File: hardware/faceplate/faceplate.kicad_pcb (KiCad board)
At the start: 2 copper layers, 9.8 x 128.5 mm, 10 parts

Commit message: New faceplate
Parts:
- removed REF** (x8): PJ398_faceplate_hole, ModularMountingKit:PJ398_faceplate_hole
- removed REF** (x2): EuroRack_MountingHole, ModularMountingKit:EuroRack_MountingHole
- added H1: Jack 1, ModularMountingHoles:6mm_Jack, F.Cu at (54.9, 66.5)
- added H10: MountingHole, ModularMountingHoles:Eurorack_mounting_hole, F.Cu at (54.0, 175.5)
- added H2: Jack 2, ModularMountingHoles:6mm_Jack, F.Cu at (54.9, 80.4)
- added H3: Jack 3, ModularMountingHoles:6mm_Jack, F.Cu at (54.9, 94.2)
- added H4: Jack 4, ModularMountingHoles:6mm_Jack, F.Cu at (54.9, 108.0)
- added H5: Jack 5, ModularMountingHoles:6mm_Jack, F.Cu at (54.9, 121.8)
- added H6: Jack 6, ModularMountingHoles:6mm_Jack, F.Cu at (54.9, 135.7)
- added H7: Jack 7, ModularMountingHoles:6mm_Jack, F.Cu at (54.9, 149.5)
- added H8: Jack 8, ModularMountingHoles:6mm_Jack, F.Cu at (54.9, 163.3)
- added H9: MountingHole, ModularMountingHoles:Eurorack_mounting_hole, F.Cu at (54.0, 53.0)

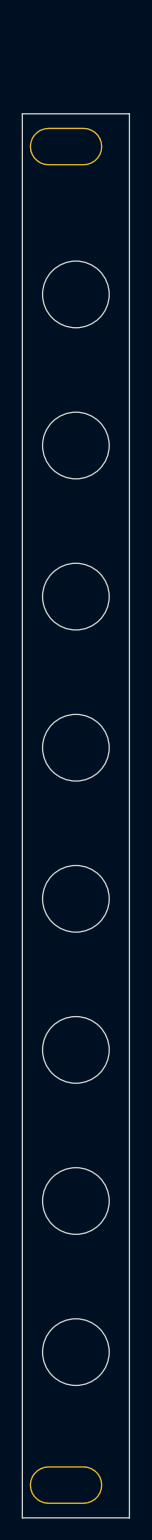
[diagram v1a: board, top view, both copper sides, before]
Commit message: Updated faceplate
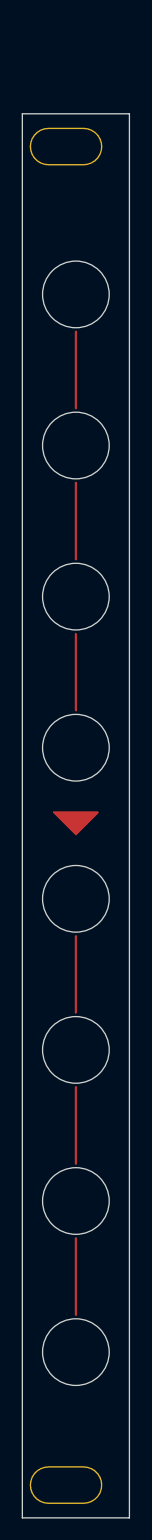
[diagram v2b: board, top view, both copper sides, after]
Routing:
- net (no net): track 0.00 -> 42.0 mm
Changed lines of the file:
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@@
 		(embedded_fonts no)
+	)
+	(gr_poly
+		(pts
+			(xy 52.9 113.93) (xy 56.9 113.93) (xy 54.9 115.93)
+		)
+		(stroke
+			(width 0.2)
+			(type solid)
+		)
+		(fill yes)
+		(layer "F.Cu")
+	)
+	(gr_poly
+		(pts
+			(xy 52.9 113.93) (xy 56.9 113.93) (xy 54.9 115.93)
+		)
+		(stroke
+			(width 0.2)
+			(type solid)
+		)
+		(fill yes)
+		(layer "F.Mask")
+	)
+	(gr_line
+		(start 54.9 125.258572)
+		(end 54.9 132.258572)
+		(stroke
+			(width 0.2)
+			(type solid)
+		)
+		(layer "F.Mask")
+	)
+	(gr_line
+		(start 54.9 139.087143)
+		(end 54.9 146.087143)
+		(stroke
+			(width 0.2)
+			(type solid)
+		)
+		(layer "F.Mask")
+	)
+	(gr_line
+		(start 54.9 69.944286)
+		(end 54.9 76.944286)
+		(stroke
+			(width 0.2)
+			(type solid)
+		)
+		(layer "F.Mask")
+	)
+	(gr_line
+		(start 54.9 97.601429)
+		(end 54.9 104.601429)
+		(stroke
+			(width 0.2)
+			(type solid)
+		)
+		(layer "F.Mask")
+	)
+	(gr_line
+		(start 54.9 83.772857)
+		(end 54.9 90.772857)
+		(stroke
+			(width 0.2)
+			(type solid)
+		)
+		(layer "F.Mask")
+	)
+	(gr_line
+		(start 54.9 152.915715)
+		(end 54.9 159.915715)
+		(stroke
+			(width 0.2)
+			(type solid)
+		)
+		(layer "F.Mask")
 	)
 	(gr_rect
@@
 		(layer "Edge.Cuts")
 	)
+	(segment
+		(start 54.9 125.258572)
+		(end 54.9 132.258572)
+		(width 0.2)
+		(locked yes)
+		(layer "F.Cu")
+		(net 0)
+	)
+	(segment
+		(start 54.9 139.087143)
+		(end 54.9 146.087143)
+		(width 0.2)
+		(locked yes)
+		(layer "F.Cu")
+		(net 0)
+	)
+	(segment
+		(start 54.9 97.601429)
+		(end 54.9 104.601429)
+		(width 0.2)
+		(locked yes)
+		(layer "F.Cu")
+		(net 0)
+	)
+	(segment
+		(start 54.9 69.944286)
+		(end 54.9 76.944286)
+		(width 0.2)
+		(locked yes)
+		(layer "F.Cu")
+		(net 0)
+	)
+	(segment
+		(start 54.9 152.915715)
+		(end 54.9 159.915715)
+		(width 0.2)
+		(locked yes)
+		(layer "F.Cu")
+		(net 0)
+	)
+	(segment
+		(start 54.9 83.772857)
+		(end 54.9 90.772857)
+		(width 0.2)
+		(locked yes)
+		(layer "F.Cu")
+		(net 0)
+	)
 	(embedded_fonts no)
